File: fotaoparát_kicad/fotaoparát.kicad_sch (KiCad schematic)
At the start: 13 parts, among them IC1 W25Q256JVEIQ, J1 Conn_01x15_Pin, J2 Micro_SD_Card_Det1, Q1 AO3400A

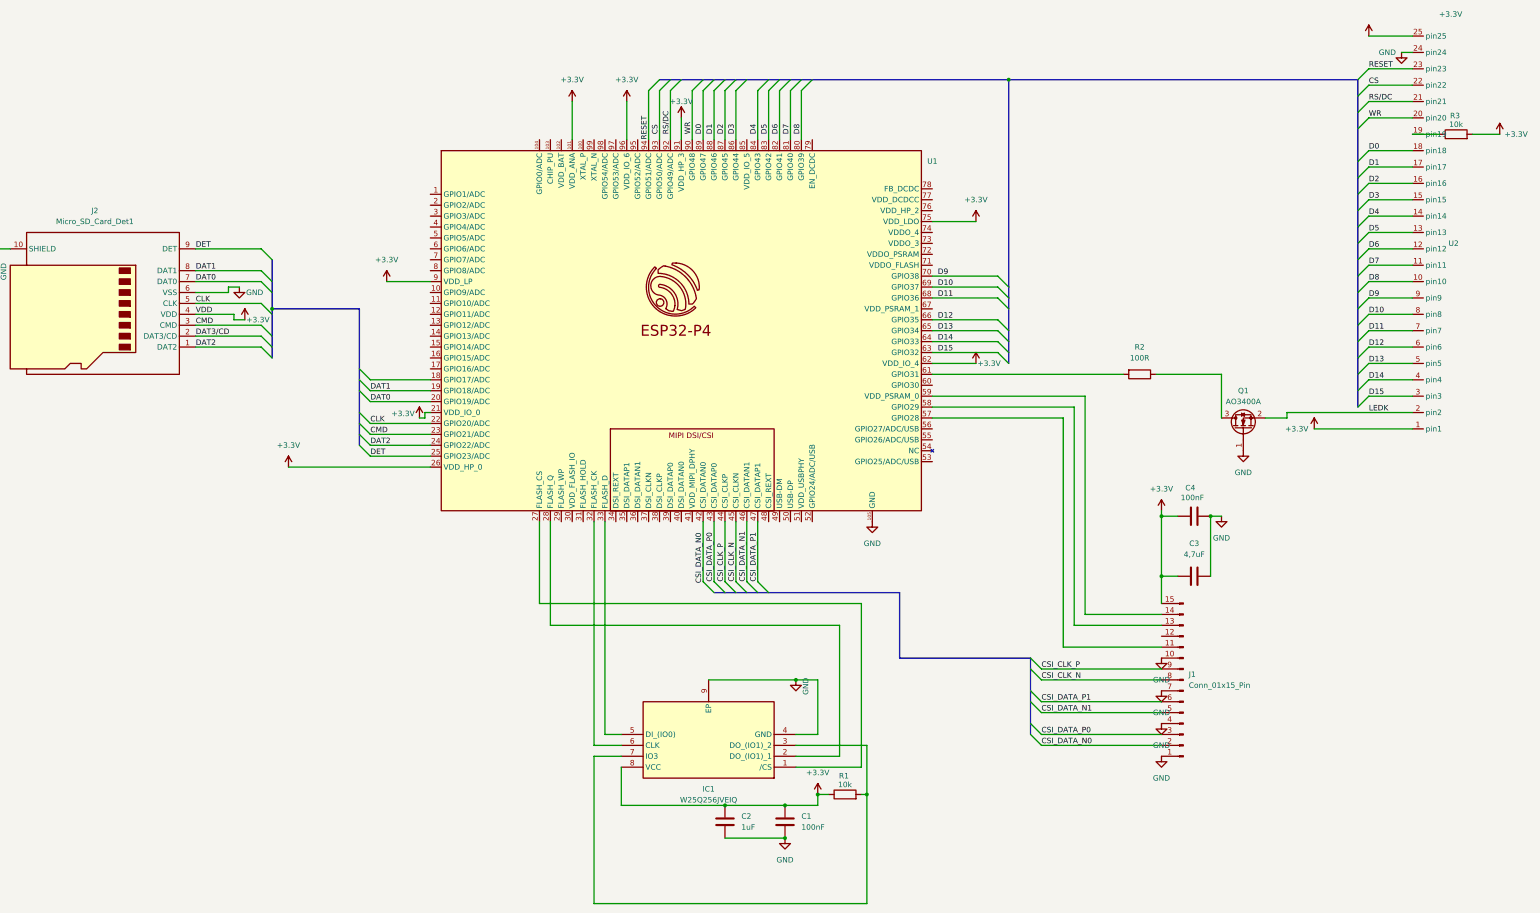
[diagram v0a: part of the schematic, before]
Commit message: Tech zmen je tolik ze ani nevim co napsat Rerouting v podstate vseho, znovu predelani displaye, flash, sd kartoveho holderu
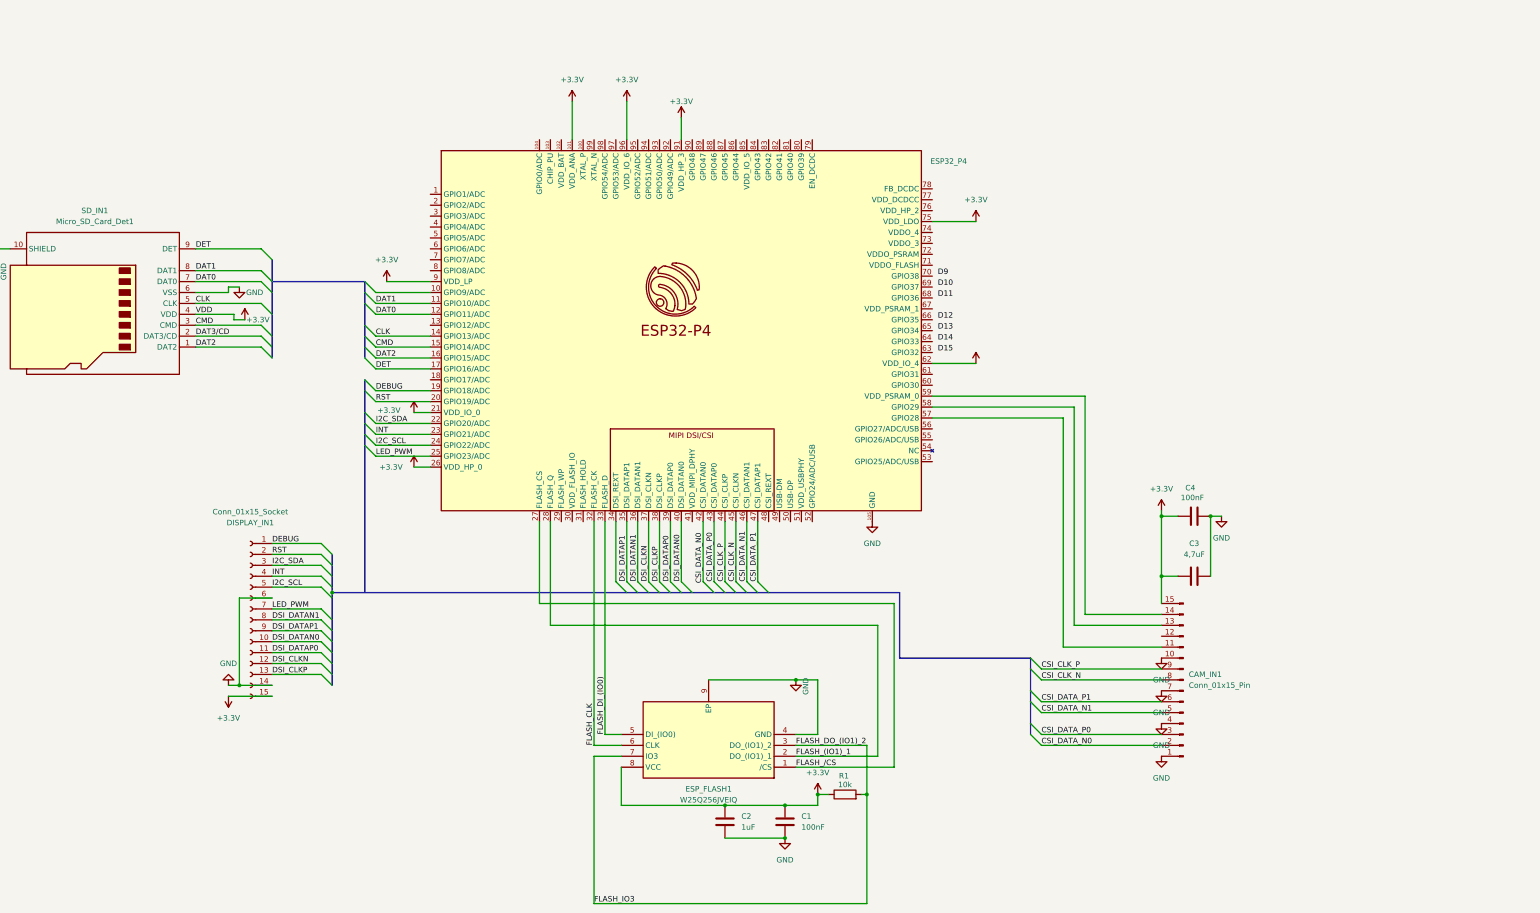
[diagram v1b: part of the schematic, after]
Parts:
- removed Q1: AO3400A, Package_TO_SOT_SMD:SOT-23, symbol Transistor_FET:AO3400A
- removed R2: 100R, Resistor_SMD:R_0603_1608Metric, symbol Device:R
- removed R3: 10k, Resistor_SMD:R_0603_1608Metric, symbol Device:R
- removed U2: ~, Connector_FFC-FPC:Hirose_FH12-40S-0.5SH_1x40-1MP_P0.50mm_Horizontal, symbol st_lib:ST7796s
- added DISPLAY_IN1: Conn_01x15_Socket, Connector_FFC-FPC:Hirose_FH12-15S-0.5SH_1x15-1MP_P0.50mm_Horizontal, symbol Connector:Conn_01x15_Socket
- renumbered J1 to CAM_IN1, U1 to ESP32_P4, IC1 to ESP_FLASH1, J2 to SD_IN1
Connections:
- net +3.3V: now also DISPLAY_IN1.15 (Pin_15)
- net CLK: now also ESP32_P4.14 (GPIO13/ADC); no longer ESP32_P4.22 (GPIO20/ADC)
- net CMD: now also ESP32_P4.15 (GPIO14/ADC); no longer ESP32_P4.23 (GPIO21/ADC)
- net D10: no longer ESP32_P4.69 (GPIO37)
- net D11: no longer ESP32_P4.68 (GPIO36)
- net D12: no longer ESP32_P4.66 (GPIO35)
- net D13: no longer ESP32_P4.65 (GPIO34)
- net D14: no longer ESP32_P4.64 (GPIO33)
- net D15: no longer ESP32_P4.63 (GPIO32)
- net D9: no longer ESP32_P4.70 (GPIO38)
- net DAT0: now also ESP32_P4.12 (GPIO11/ADC); no longer ESP32_P4.20 (GPIO19/ADC)
- net DAT1: now also ESP32_P4.11 (GPIO10/ADC); no longer ESP32_P4.19 (GPIO18/ADC)
- net DAT2: now also ESP32_P4.16 (GPIO15/ADC); no longer ESP32_P4.24 (GPIO22/ADC)
- net DET: now also ESP32_P4.17 (GPIO16/ADC); no longer ESP32_P4.25 (GPIO23/ADC)
- net GND: now also DISPLAY_IN1.14 (Pin_14), DISPLAY_IN1.6 (Pin_6)
- net FLASH_/CS: now reaches ESP32_P4.27 (FLASH_CS), ESP_FLASH1.1 (/CS)
- net FLASH_(IO1)_1: now reaches ESP32_P4.28 (FLASH_Q), ESP_FLASH1.2 (DO_(IO1)_1)
- net FLASH_CLK: now reaches ESP32_P4.32 (FLASH_CK), ESP_FLASH1.6 (CLK)
- net FLASH_DI_(IO0): now reaches ESP32_P4.33 (FLASH_D), ESP_FLASH1.5 (DI_(IO0))
- net DSI_DATAP1: now reaches ESP32_P4.35 (DSI_DATAP1)
- net DSI_DATAP1: now also DISPLAY_IN1.9 (Pin_9)
- net DSI_DATAN1: now reaches ESP32_P4.36 (DSI_DATAN1)
- net DSI_DATAN1: now also DISPLAY_IN1.8 (Pin_8)
- net DSI_CLKN: now reaches ESP32_P4.37 (DSI_CLKN)
- net DSI_CLKN: now also DISPLAY_IN1.12 (Pin_12)
- net DSI_CLKP: now reaches ESP32_P4.38 (DSI_CLKP)
- net DSI_CLKP: now also DISPLAY_IN1.13 (Pin_13)
- net DSI_DATAP0: now reaches ESP32_P4.39 (DSI_DATAP0)
- net DSI_DATAP0: now also DISPLAY_IN1.11 (Pin_11)
- net DSI_DATAN0: now reaches ESP32_P4.40 (DSI_DATAN0)
- net DSI_DATAN0: now also DISPLAY_IN1.10 (Pin_10)
- net FLASH_DO_(IO1)_2: now reaches ESP_FLASH1.3 (DO_(IO1)_2), ESP_FLASH1.7 (IO3), R1.2
- net CS: no longer names the net of ESP32_P4.93 (GPIO50/ADC)
- net D0: no longer names the net of ESP32_P4.89 (GPIO47)
- net D1: no longer names the net of ESP32_P4.88 (GPIO46)
- net D2: no longer names the net of ESP32_P4.87 (GPIO45)
- net D3: no longer names the net of ESP32_P4.86 (GPIO44)
- net D4: no longer names the net of ESP32_P4.84 (GPIO43)
- net D5: no longer names the net of ESP32_P4.83 (GPIO42)
- net D6: no longer names the net of ESP32_P4.82 (GPIO41)
- net D7: no longer names the net of ESP32_P4.81 (GPIO40)
- net D8: no longer names the net of ESP32_P4.80 (GPIO39)
- net RESET: no longer names the net of ESP32_P4.94 (GPIO51/ADC)
- net RS/DC: no longer names the net of ESP32_P4.92 (GPIO49/ADC)
- net WR: no longer names the net of ESP32_P4.90 (GPIO48)
- new net DEBUG: DISPLAY_IN1.1 (Pin_1), ESP32_P4.19 (GPIO18/ADC)
- new net I2C_SCL: DISPLAY_IN1.5 (Pin_5), ESP32_P4.24 (GPIO22/ADC)
- new net I2C_SDA: DISPLAY_IN1.3 (Pin_3), ESP32_P4.22 (GPIO20/ADC)
- new net INT: DISPLAY_IN1.4 (Pin_4), ESP32_P4.23 (GPIO21/ADC)
- new net LED_PWM: DISPLAY_IN1.7 (Pin_7), ESP32_P4.25 (GPIO23/ADC)
- new net RST: DISPLAY_IN1.2 (Pin_2), ESP32_P4.20 (GPIO19/ADC)

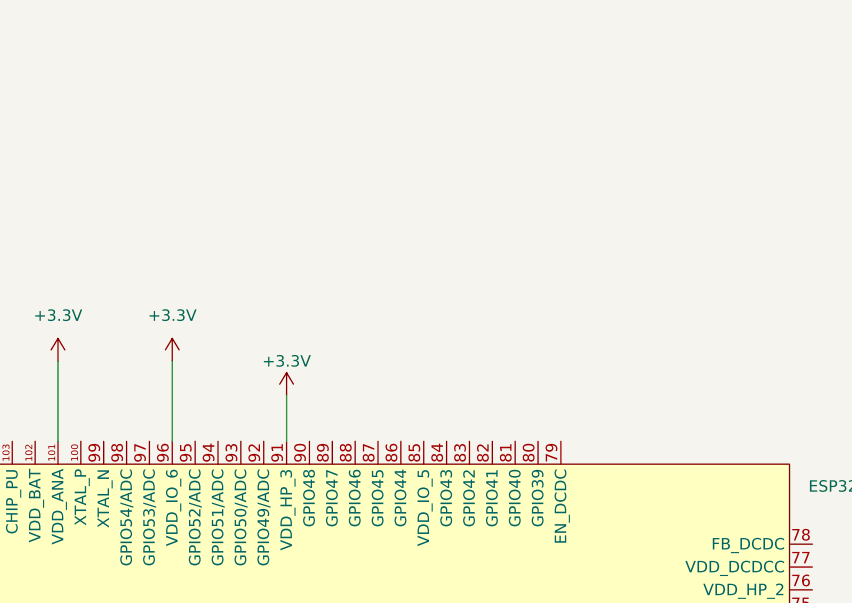
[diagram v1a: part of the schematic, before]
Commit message: delani pullups
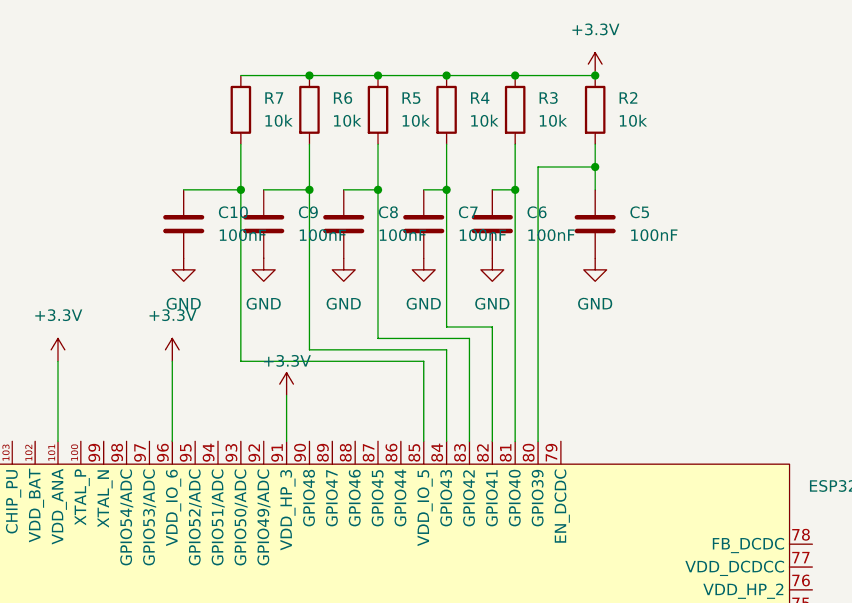
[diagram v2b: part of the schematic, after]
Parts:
- added C10, C5, C6, C7, C8, C9: 100nF, Capacitor_SMD:C_0201_0603Metric, symbol Device:C
- added R2, R3, R4, R5, R6, R7: 10k, Resistor_SMD:R_0603_1608Metric, symbol Device:R
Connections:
- net +3.3V: now also R2.1, R3.1, R4.1, R5.1, R6.1, R7.1
- net GND: now also C10.2, C5.2, C6.2, C7.2, C8.2, C9.2
- net at ESP32_P4.80 (GPIO39): now also C5.1, R2.2
- net at ESP32_P4.81 (GPIO40): now also C6.1, R3.2
- net at ESP32_P4.82 (GPIO41): now also C7.1, R4.2
- net at ESP32_P4.83 (GPIO42): now also C8.1, R5.2
- net at ESP32_P4.84 (GPIO43): now also C9.1, R6.2
- net at ESP32_P4.85 (VDD_IO_5): now also C10.1, R7.2

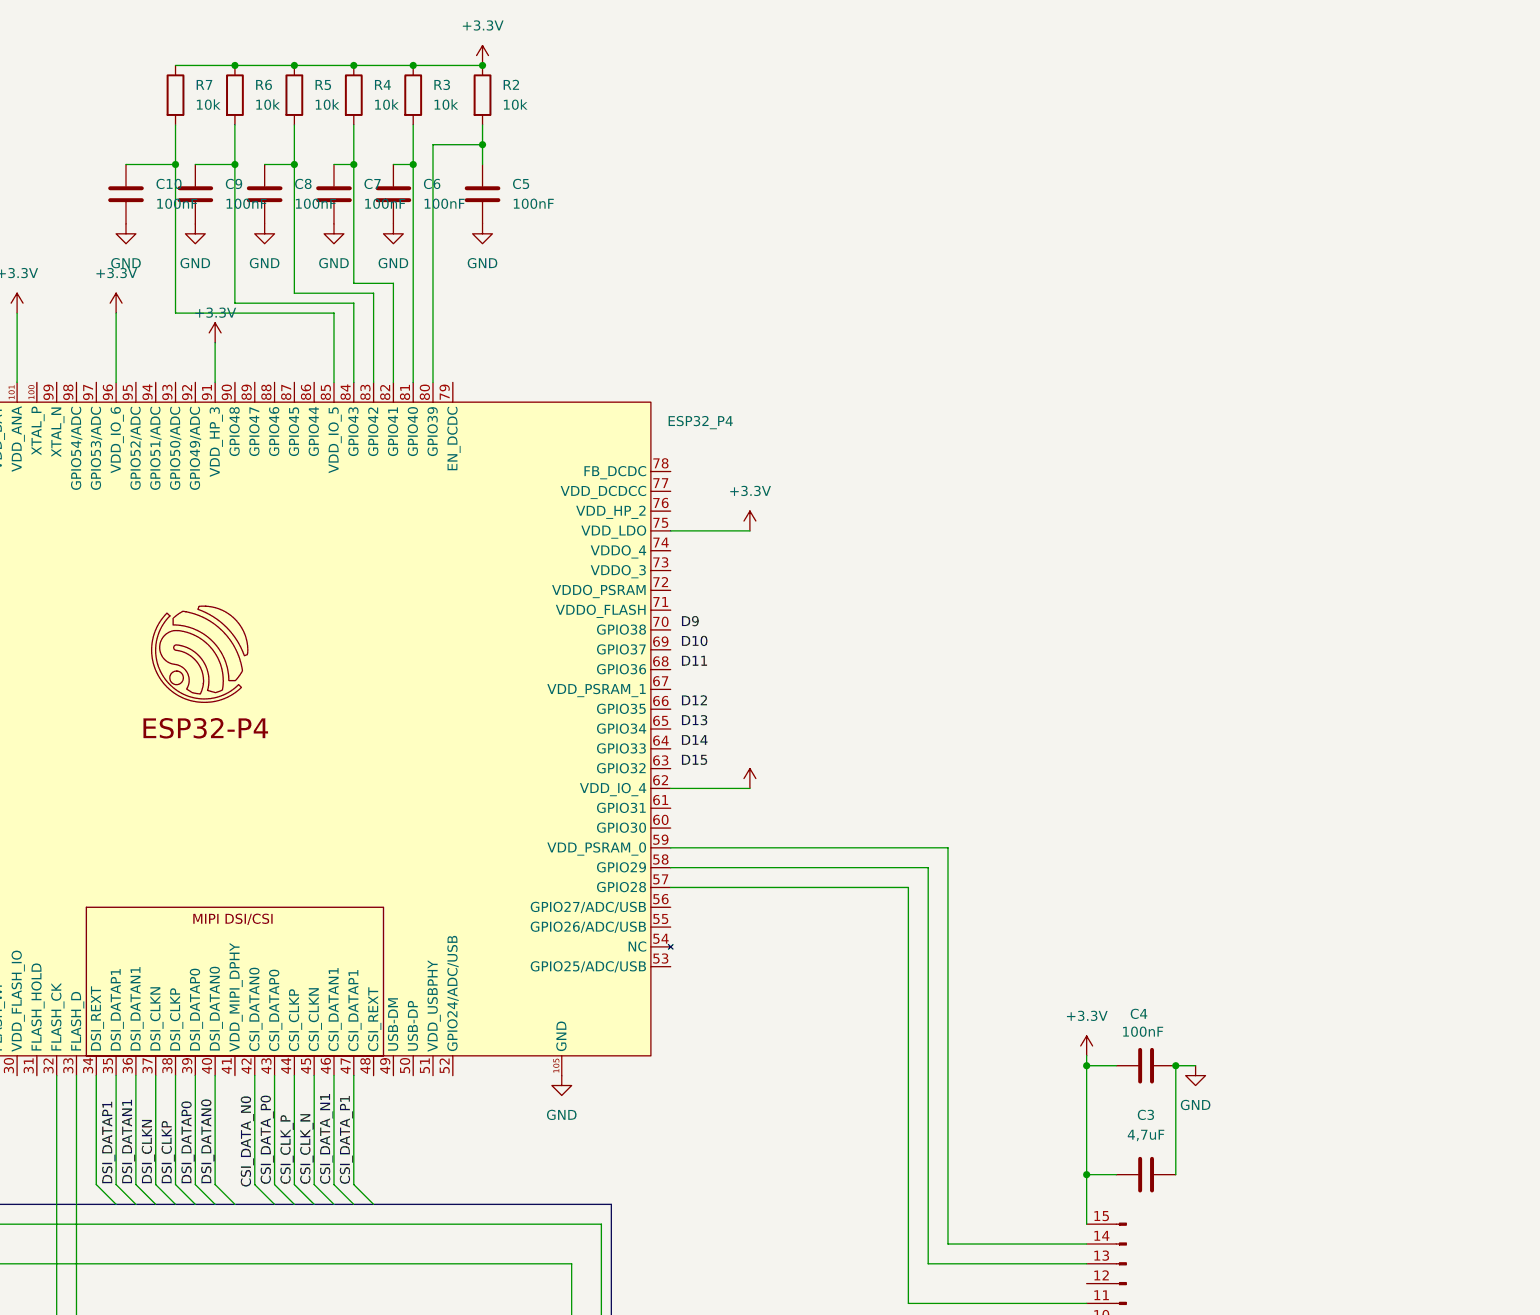
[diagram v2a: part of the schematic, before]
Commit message: delal jsem pullups
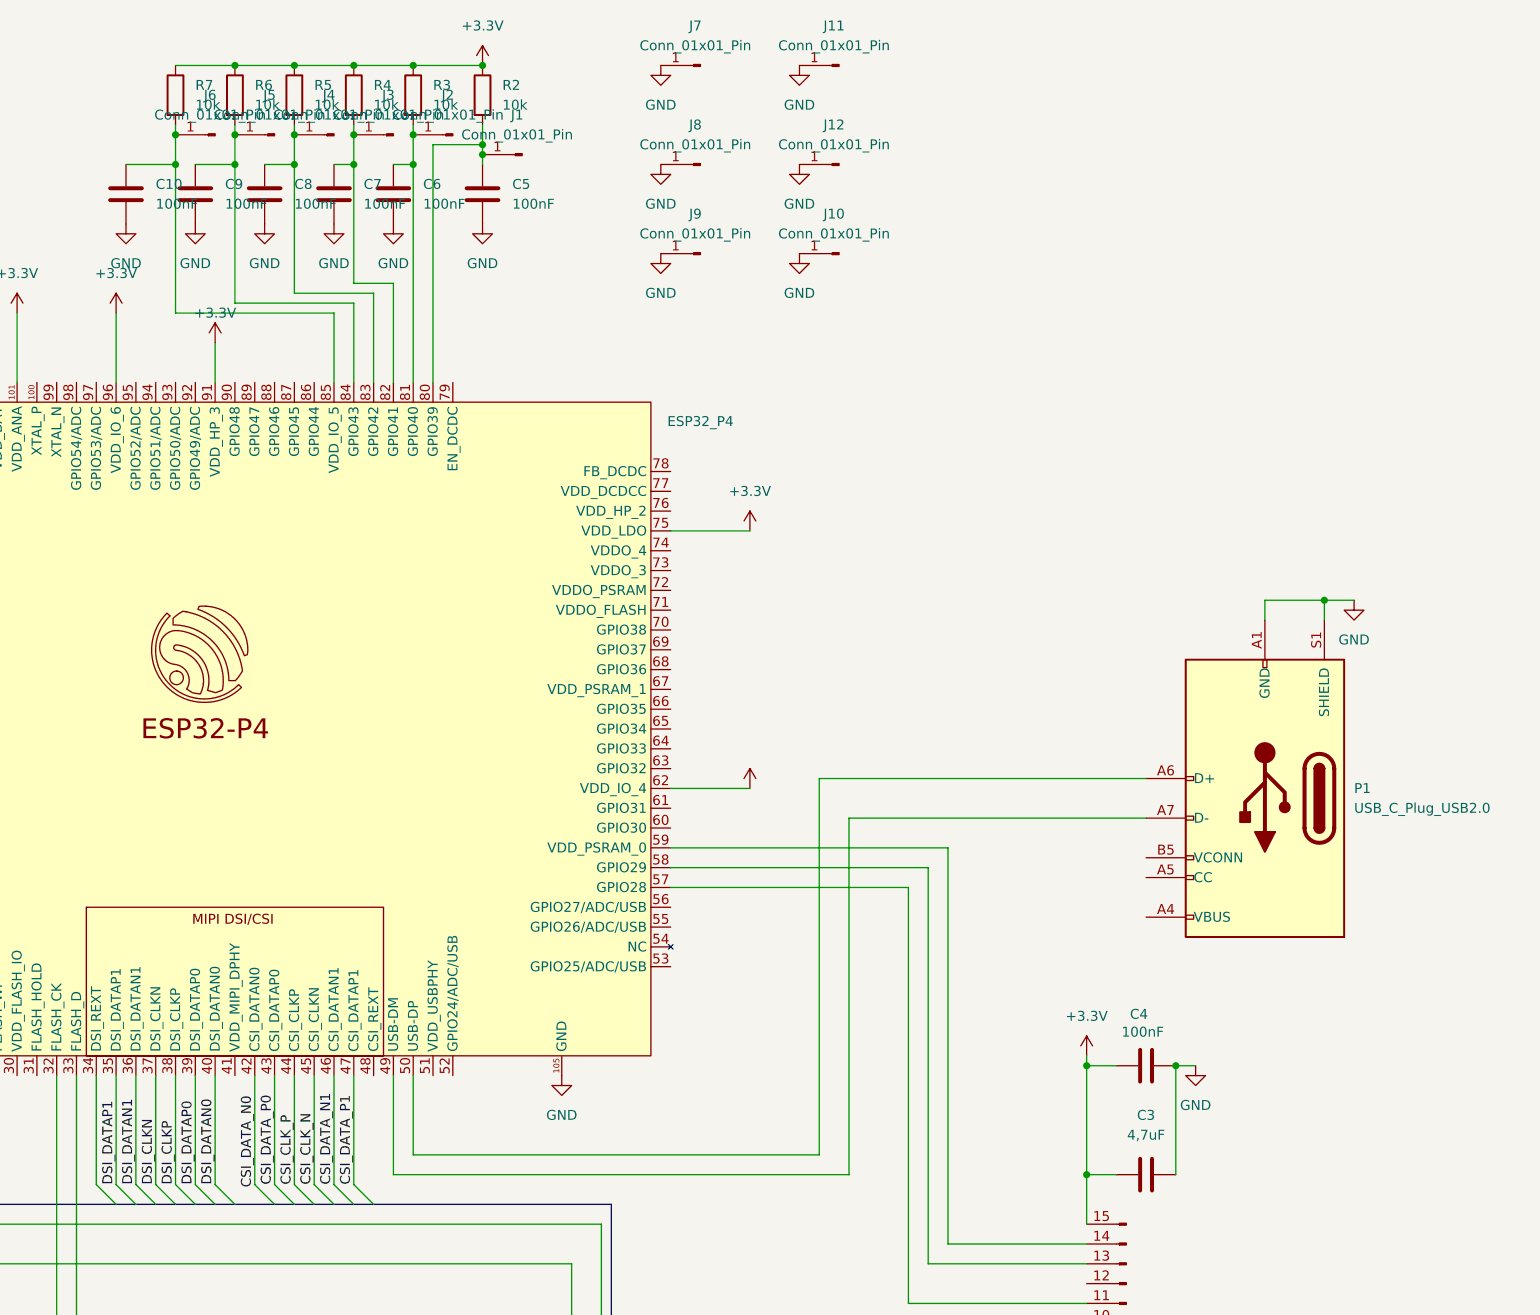
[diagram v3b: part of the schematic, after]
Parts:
- added J1, J10, J11, J12, J2, J3, J4, J5, J6, J7, J8, J9: Conn_01x01_Pin, Connector_Wire:SolderWire-1.5sqmm_1x01_D1.7mm_OD3.9mm, symbol Connector:Conn_01x01_Pin
- added P1: USB_C_Plug_USB2.0, Connector_USB:USB_C_Plug_Molex_105444, symbol Connector:USB_C_Plug_USB2.0
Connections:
- net GND: now also J10.1 (Pin_1), J11.1 (Pin_1), J12.1 (Pin_1), J7.1 (Pin_1), J8.1 (Pin_1), J9.1 (Pin_1), P1.A1 (GND), P1.A12 (GND), P1.B1 (GND), P1.B12 (GND), P1.S1 (SHIELD)
- net at C9.1, ESP32_P4.84 (GPIO43), R6.2: now also J5.1 (Pin_1)
- net at C8.1, ESP32_P4.83 (GPIO42), R5.2: now also J4.1 (Pin_1)
- net at C5.1, ESP32_P4.80 (GPIO39), R2.2: now also J1.1 (Pin_1)
- net at C6.1, ESP32_P4.81 (GPIO40), R3.2: now also J2.1 (Pin_1)
- net at C10.1, ESP32_P4.85 (VDD_IO_5), R7.2: now also J6.1 (Pin_1)
- net at ESP32_P4.49 (USB-DM): now also P1.A7 (D-)
- net at ESP32_P4.50 (USB-DP): now also P1.A6 (D+)
- net at C7.1, ESP32_P4.82 (GPIO41), R4.2: now also J3.1 (Pin_1)
- new net: P1.A4 (VBUS), P1.A9 (VBUS), P1.B4 (VBUS), P1.B9 (VBUS)
